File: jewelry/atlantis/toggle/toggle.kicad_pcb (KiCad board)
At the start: 2 copper layers, 24 x 24 mm, 11 parts, among them Q1 Q_PMOS_DGS, U1 74LVC2G04

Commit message: atlantis: Rough PCB for earthing
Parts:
- removed R3: R, Resistor_SMD:R_0603_1608Metric_Pad1.05x0.95mm_HandSolder
- added D10: LED, LED_SMD:LED_0603_1608Metric_Pad1.05x0.95mm_HandSolder, F.Cu at (94.0, 64.8)
- added D11: LED, LED_SMD:LED_0603_1608Metric_Pad1.05x0.95mm_HandSolder, F.Cu at (97.8, 62.2)
- added D12: LED, LED_SMD:LED_0603_1608Metric_Pad1.05x0.95mm_HandSolder, F.Cu at (102.9, 62.2)
- added D4: LED, LED_SMD:LED_0603_1608Metric_Pad1.05x0.95mm_HandSolder, F.Cu at (77.5, 85.5)
- added D5: LED, LED_SMD:LED_0603_1608Metric_Pad1.05x0.95mm_HandSolder, F.Cu at (78.7, 80.9)
- added D6: LED, LED_SMD:LED_0603_1608Metric_Pad1.05x0.95mm_HandSolder, F.Cu at (81.3, 77.5)
- added D7: LED, LED_SMD:LED_0603_1608Metric_Pad1.05x0.95mm_HandSolder, F.Cu at (83.8, 73.7)
- added D8: LED, LED_SMD:LED_0603_1608Metric_Pad1.05x0.95mm_HandSolder, F.Cu at (86.4, 69.8)
- added D9: LED, LED_SMD:LED_0603_1608Metric_Pad1.05x0.95mm_HandSolder, F.Cu at (88.9, 66.9)
- added L1: L, Inductor_SMD:L_1206_3216Metric_Pad1.42x1.75mm_HandSolder, F.Cu at (92.7, 118.1)
- added SW1: SW_SPST, Button_Switch_SMD:SW_SPST_B3S-1000, F.Cu at (80.0, 111.8)
- BT1: value Battery_Cell -> CR1216; footprint Battery:Battery_Panasonic_CR1220-VCN_Vertical_CircularHoles -> touchled:Battery_CR1225
- C1: value 1nF -> 1uF
- C2: value 100nF -> 1uF
- Q1: value Q_PMOS_DGS -> BSS138L
- R1: value 10k -> 100k
- R2: value 100k -> 220R
- U1: value 74LVC2G04 -> AP3019A; footprint Package_TO_SOT_SMD:SOT-23-6_Handsoldering -> touchled:SOT-223-6-extraspace
- moved U1 40.4 mm to (98.0, 117.3), turned to 145 degrees
- moved R2 37.2 mm to (101.6, 119.4), turned to 235 degrees
- moved BT1 35.4 mm to (115.6, 66.0), turned to 315 degrees
- moved C2 32.2 mm to (99.1, 114.3), turned to 325 degrees
- moved Q1 30.7 mm to (89.7, 111.7), turned to 145 degrees
- moved C1 30.0 mm to (88.9, 115.6), turned to 145 degrees
- moved R1 29.3 mm to (94.7, 115.0), turned to 55 degrees
- moved D1 21.4 mm to (77.5, 101.2), turned to 300 degrees
- moved D3 18.6 mm to (77.5, 90.2), turned to 270 degrees
- moved D2 9.39 mm to (77.5, 95.2), turned to 290 degrees
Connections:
- BT1 pad 2: GND -> Net-(BT1-Pad2)
- C1 pad 1: Net-(C1-Pad1) -> VCC
- C2 pad 1: Net-(C2-Pad1) -> /LED+
- D1 pad 1: GND -> Net-(D1-Pad1)
- D1 pad 2: Net-(D1-Pad2) -> /LED+
- D2 pad 1: GND -> Net-(D1-Pad1)
- D2 pad 2: Net-(D1-Pad2) -> /LED+
- D3 pad 1: GND -> Net-(D3-Pad1)
- D3 pad 2: Net-(D1-Pad2) -> Net-(D1-Pad1)
- Q1 pad 1: Net-(BT1-Pad1) -> GND
- Q1 pad 2: GND -> Net-(BT1-Pad2)
- Q1 pad 3: VCC -> Net-(BT1-Pad1)
- R1 pad 1: /OUT -> VCC
- R1 pad 2: Net-(C1-Pad1) -> Net-(R1-Pad2)
- R2 pad 1: Net-(R2-Pad1) -> /LED-
- R2 pad 2: Net-(C2-Pad1) -> GND
- U1 pad 1: Net-(C1-Pad1) -> Net-(L1-Pad2)
- U1 pad 3: Net-(R2-Pad1) -> /LED-
- U1 pad 4: /OUT -> Net-(R1-Pad2)
- U1 pad 5: VCC -> /LED+
- U1 pad 6: Net-(R2-Pad1) -> VCC
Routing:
- net GND: track 0.00 -> 32.3 mm
- net /LED+: track 0.00 -> 30.5 mm
- net Net-(D1-Pad1): track 0.00 -> 15.6 mm
- net Net-(D10-Pad1): track 0.00 -> 15.6 mm
- net Net-(D3-Pad1): track 0.00 -> 14.2 mm
- net Net-(D5-Pad1): track 0.00 -> 13.7 mm
- net Net-(D10-Pad2): track 0.00 -> 13.3 mm
- net VCC: track 0.00 -> 8.44 mm
- net Net-(D11-Pad1): track 0.00 -> 6.43 mm
- net Net-(L1-Pad2): track 0.00 -> 4.52 mm
- net /LED-: track 0.00 -> 3.01 mm
- net Net-(R1-Pad2): track 0.00 -> 2.79 mm
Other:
- board size 24 x 24 mm -> 49.4 x 67.3 mm

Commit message: atlantis: More rough PCB
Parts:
- SW1: footprint Button_Switch_SMD:SW_SPST_B3S-1000 -> Button_Switch_SMD:SW_SPDT_PCM12
- moved SW1 1.27 mm to (81.3, 111.8), turned to 325 degrees
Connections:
- D11 pad 1: Net-(D11-Pad1) -> /LED-
- D12 pad 1: Net-(D11-Pad1) -> /LED-
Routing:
- net /LED-: track 3.01 -> 79.9 mm
- net Net-(D11-Pad1): track 6.43 -> 0.00 mm
- net /LED+: track 30.5 -> 31.6 mm
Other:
- net class Default: clearance 0.2 -> 0.4; trace_width 0.25 -> 0.4
- rule trace_clearance: 0.2 -> 0.4

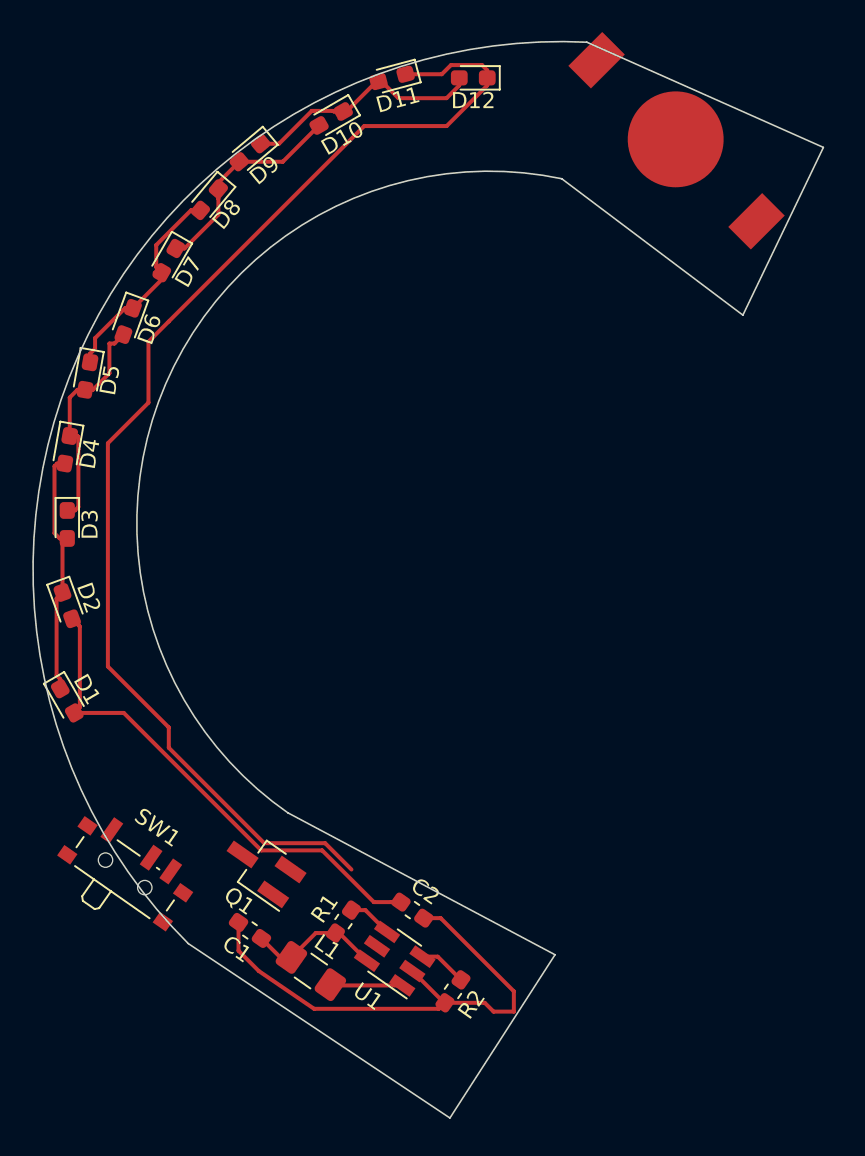
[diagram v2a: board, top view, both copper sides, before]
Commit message: atlantis: Backimport PCB for earthing
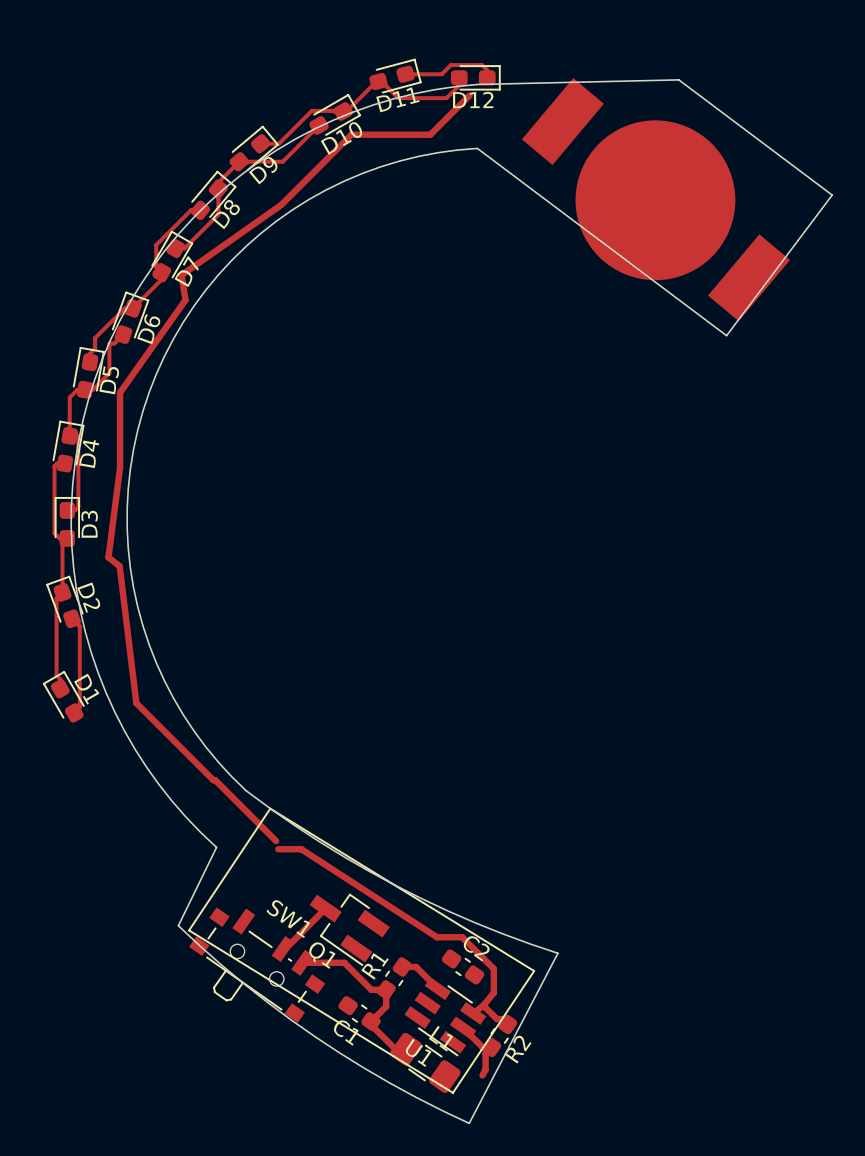
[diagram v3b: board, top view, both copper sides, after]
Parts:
- SW1: value SW_SPST -> SW_SPDT
- moved SW1 10.0 mm to (89.5, 117.5)
- moved L1 9.19 mm to (99.9, 123.9)
- moved C1 8.61 mm to (95.8, 120.8)
- moved Q1 6.21 mm to (94.9, 115.1)
- moved C2 4.77 mm to (102.2, 117.9)
- moved R1 4.77 mm to (97.9, 118.6)
- moved U1 4.77 mm to (101.1, 120.9)
- moved R2 4.04 mm to (104.5, 122.2)
- moved BT1 4.02 mm to (114.3, 69.8), turned to 320 degrees
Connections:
- SW1 pad 1: Net-(BT1-Pad1) -> Net-(SW1-Pad1)
- SW1 pad 2: VCC -> Net-(BT1-Pad1)
- SW1 pad 3: (no net) -> VCC
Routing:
- net GND: track 32.3 -> 4.25 mm
- net /LED+: track 31.6 -> 6.24 mm
- net /LED-: track 79.9 -> 90.4 mm
- net Net-(L1-Pad2): track 4.52 -> 0.00 mm
- net Net-(BT1-Pad1): track 0.00 -> 3.72 mm
- net VCC: track 8.44 -> 11.2 mm
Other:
- board size 49.4 x 67.3 mm -> 47.6 x 65.3 mm

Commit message: atlantis: Earthing PCB near ready
Just positioning and routing of LEDs
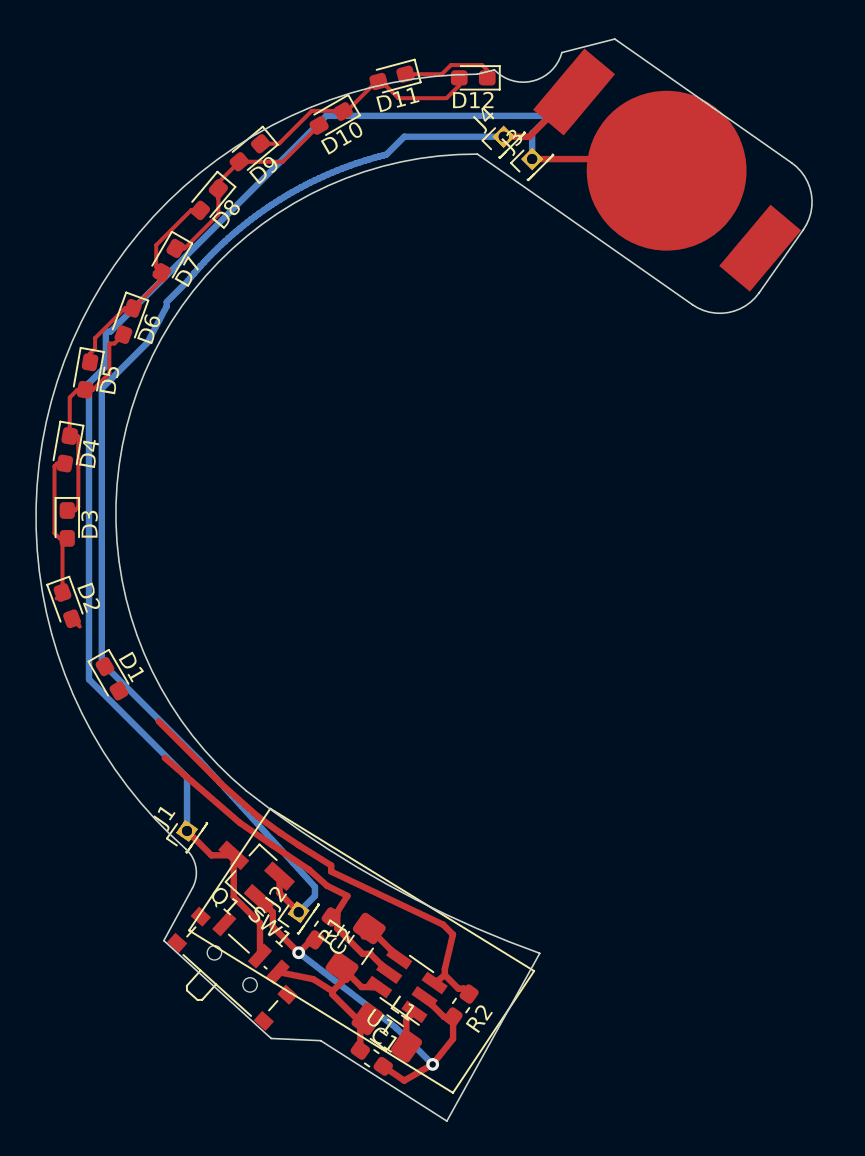
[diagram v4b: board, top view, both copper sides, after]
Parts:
- added J1: Conn_01x01, Connector_PinHeader_1.27mm:PinHeader_1x01_P1.27mm_Vertical, F.Cu at (85.0, 109.3)
- added J2: Conn_01x01, Connector_PinHeader_1.27mm:PinHeader_1x01_P1.27mm_Vertical, F.Cu at (91.9, 114.4)
- added J3: Conn_01x01, Connector_PinHeader_1.27mm:PinHeader_1x01_P1.27mm_Vertical, F.Cu at (106.6, 67.3)
- added J4: Conn_01x01, Connector_PinHeader_1.27mm:PinHeader_1x01_P1.27mm_Vertical, F.Cu at (104.8, 65.9)
- R1: footprint Resistor_SMD:R_0603_1608Metric_Pad1.05x0.95mm_HandSolder -> Resistor_SMD:R_1206_3216Metric_Pad1.42x1.75mm_HandSolder
- moved C2 9.09 mm to (93.5, 115.4), turned to 235 degrees
- moved Q1 6.68 mm to (89.0, 111.9), turned to 138 degrees
- moved D1 3.12 mm to (80.3, 99.8)
- moved L1 3.07 mm to (97.5, 122.0)
- moved R2 3.07 mm to (102.1, 120.3)
- moved U1 3.07 mm to (98.7, 119.0)
- moved R1 3.07 mm to (95.5, 116.7)
- moved C1 2.90 mm to (96.5, 123.6), turned to 325 degrees
- moved BT1 1.98 mm to (115.0, 68.0)
- moved SW1 1.55 mm to (88.0, 117.7), turned to 318 degrees
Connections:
- net Net-(BT1-Pad1) renamed /BATT+
- net Net-(BT1-Pad2) renamed /BATT-
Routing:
- net /BATT+: track 3.72 -> 90.0 mm
- net /BATT-: track 0.00 -> 78.4 mm
- net /LED-: track 90.4 -> 34.5 mm
- net GND: track 4.25 -> 26.0 mm, vias 0 -> 2
- net /LED+: track 6.24 -> 21.7 mm
- net Net-(D1-Pad1): track 15.6 -> 9.88 mm
- net VCC: track 11.2 -> 13.8 mm
- net Net-(L1-Pad2): track 0.00 -> 2.36 mm
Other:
- board size 47.6 x 65.3 mm -> 48.5 x 67.7 mm

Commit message: atlantis: Earthing PCB ready for test?
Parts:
- moved D12 4.12 mm to (99.4, 64.5), turned to 10 degrees
- moved D11 4.02 mm to (95.5, 65.5), turned to 20 degrees
- moved D10 3.42 mm to (91.7, 67.3), turned to 28 degrees
- moved D8 2.56 mm to (85.2, 72.1), turned to 45 degrees
- moved D9 2.48 mm to (88.4, 69.3), turned to 37 degrees
- moved D7 2.08 mm to (82.5, 75.3), turned to 55 degrees
- moved D5 1.94 mm to (79.0, 82.8), turned to 75 degrees
- moved D4 1.63 mm to (78.1, 87.0), turned to 83 degrees
- moved D6 1.59 mm to (80.5, 78.9), turned to 65 degrees
- moved D1 1.08 mm to (79.5, 99.1), turned to 110 degrees
- moved D3 1.02 mm to (78.0, 91.1), turned to 90 degrees
- moved J2 0.99 mm to (92.6, 113.7)
- moved D2 0.90 mm to (78.4, 95.1), turned to 100 degrees
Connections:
- D1 pad 1: Net-(D1-Pad1) -> /LED-
- D1 pad 2: /LED+ -> Net-(D1-Pad2)
- D11 pad 1: /LED- -> Net-(D10-Pad2)
- D11 pad 2: Net-(D10-Pad1) -> /LED+
- D12 pad 1: /LED- -> Net-(D10-Pad2)
- D12 pad 2: Net-(D10-Pad1) -> /LED+
- D2 pad 1: Net-(D1-Pad1) -> /LED-
- D2 pad 2: /LED+ -> Net-(D1-Pad2)
- D3 pad 1: Net-(D3-Pad1) -> Net-(D1-Pad2)
- D3 pad 2: Net-(D1-Pad1) -> Net-(D3-Pad2)
- D4 pad 1: Net-(D3-Pad1) -> Net-(D1-Pad2)
- D4 pad 2: Net-(D1-Pad1) -> Net-(D3-Pad2)
- D5 pad 1: Net-(D5-Pad1) -> Net-(D3-Pad2)
- D5 pad 2: Net-(D3-Pad1) -> Net-(D5-Pad2)
- D6 pad 1: Net-(D5-Pad1) -> Net-(D3-Pad2)
- D6 pad 2: Net-(D3-Pad1) -> Net-(D5-Pad2)
- D7 pad 1: Net-(D10-Pad2) -> Net-(D5-Pad2)
- D7 pad 2: Net-(D5-Pad1) -> Net-(D10-Pad1)
- D8 pad 1: Net-(D10-Pad2) -> Net-(D5-Pad2)
- D8 pad 2: Net-(D5-Pad1) -> Net-(D10-Pad1)
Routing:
- net /LED+: track 21.7 -> 90.2 mm, vias 0 -> 2
- net Net-(D3-Pad1): track 14.2 -> 0.00 mm
- net Net-(D5-Pad1): track 13.7 -> 0.00 mm
- net Net-(D3-Pad2): track 0.00 -> 13.3 mm
- net Net-(D5-Pad2): track 0.00 -> 13.3 mm
- net Net-(D1-Pad2): track 0.00 -> 13.0 mm
- net Net-(D1-Pad1): track 9.88 -> 0.00 mm
- net /LED-: track 34.5 -> 38.2 mm
- net Net-(D10-Pad1): track 15.6 -> 12.6 mm
- net /BATT-: track 78.4 -> 76.5 mm
- net GND: track 26.0 -> 27.6 mm

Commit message: atlantis: Earthing CAD ready for first test
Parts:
- moved SW1 0.18 mm to (87.9, 117.9)
- turned BT1 to 325 degrees
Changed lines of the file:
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@@
   )
   (module touchled:Battery_CR1225 (layer F.Cu)
-    (at 115 68 320)
+    (at 115 68 325)
     (descr "CR1225 battery")
     (tags "battery CR1225 coin cell")
     (attr virtual)
-    (fp_text reference BT1 (at 0.000001 -1 140) (layer F.SilkS) hide
-      (effects (font (size 1 1) (thickness 0.15)))
-    )
-    (fp_text value CR1216 (at 0 0.499999 140) (layer F.Fab)
+    (fp_text reference BT1 (at 0.000001 -1 145) (layer F.SilkS) hide
+      (effects (font (size 1 1) (thickness 0.15)))
+    )
+    (fp_text value CR1216 (at 0 0.499999 145) (layer F.Fab)
       (effects (font (size 1 1) (thickness 0.15)))
     )
     (fp_circle (center 0 0) (end 7 0) (layer F.CrtYd) (width 0.1))
-    (pad 2 smd rect (at 7.6 0 320) (size 2.5 5) (layers F.Cu F.Paste F.Mask)
-      (net 11 /BATT-))
-    (pad 2 smd rect (at -7.6 0 320) (size 2.5 5) (layers F.Cu F.Paste F.Mask)
-      (net 11 /BATT-))
-    (pad 1 smd circle (at 0 0.05 320) (size 10 10) (layers F.Cu F.Paste F.Mask)
+    (pad 2 smd rect (at 7.6 0 325) (size 2.5 5) (layers F.Cu F.Paste F.Mask)
+      (net 11 /BATT-))
+    (pad 2 smd rect (at -7.6 0 325) (size 2.5 5) (layers F.Cu F.Paste F.Mask)
+      (net 11 /BATT-))
+    (pad 1 smd circle (at 0 0.05 325) (size 10 10) (layers F.Cu F.Paste F.Mask)
       (net 12 /BATT+))
     (model /home/jon/projects/personal/jewelry/atlantis/batth-cr1220.step
@@
   )
   (module Button_Switch_SMD:SW_SPDT_PCM12 (layer F.Cu)
-    (at 88.011 117.729 318)
+    (at 87.884 117.856 318)
     (descr "Ultraminiature Surface Mount Slide Switch, right-angle, https://www.ckswitches.com/media/1424/pcm.pdf")
     (attr smd)

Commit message: atlantis: Adjusted PCB
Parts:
- D1, D10, D11, D12, D2, D3, D4, D5, D6, D7, D8, D9: footprint LED_SMD:LED_0603_1608Metric_Pad1.05x0.95mm_HandSolder -> touchled:LED_0603_bigger
- J1, J2, J3, J4: footprint Connector_PinHeader_1.27mm:PinHeader_1x01_P1.27mm_Vertical -> touchled:PinHeader
- moved J2 6.08 mm to (87.2, 110.7), turned to 145 degrees
- moved Q1 1.65 mm to (90.2, 113.0), turned to 318 degrees
- moved J1 1.48 mm to (85.7, 108.1)
- moved J3 0.18 mm to (106.4, 67.4)
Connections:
- Q1 pad 1: GND -> /BATT+
- Q1 pad 3: /BATT+ -> GND
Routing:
- net /BATT+: track 89.7 -> 94.5 mm
- net /BATT-: track 76.5 -> 73.1 mm
- net Net-(D10-Pad2): track 13.1 -> 15.7 mm
- net Net-(D10-Pad1): track 12.6 -> 15.0 mm
- net Net-(D5-Pad2): track 13.3 -> 15.5 mm
- net Net-(D3-Pad2): track 13.3 -> 15.5 mm
- net Net-(D1-Pad2): track 13.0 -> 15.0 mm
- net /LED+: track 90.2 -> 91.8 mm
- net /LED-: track 38.2 -> 39.4 mm

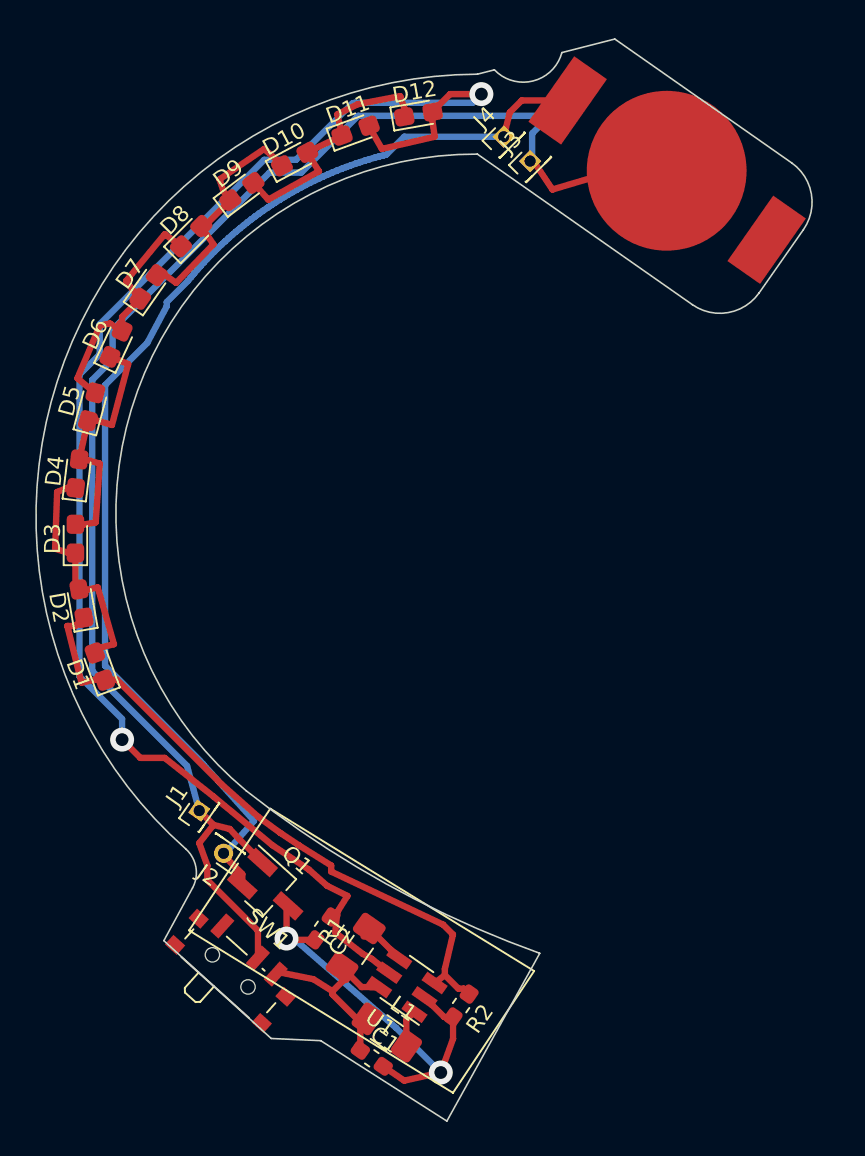
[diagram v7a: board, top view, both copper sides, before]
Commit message: atlantis: Fix batt holder and NMOS wrong direction
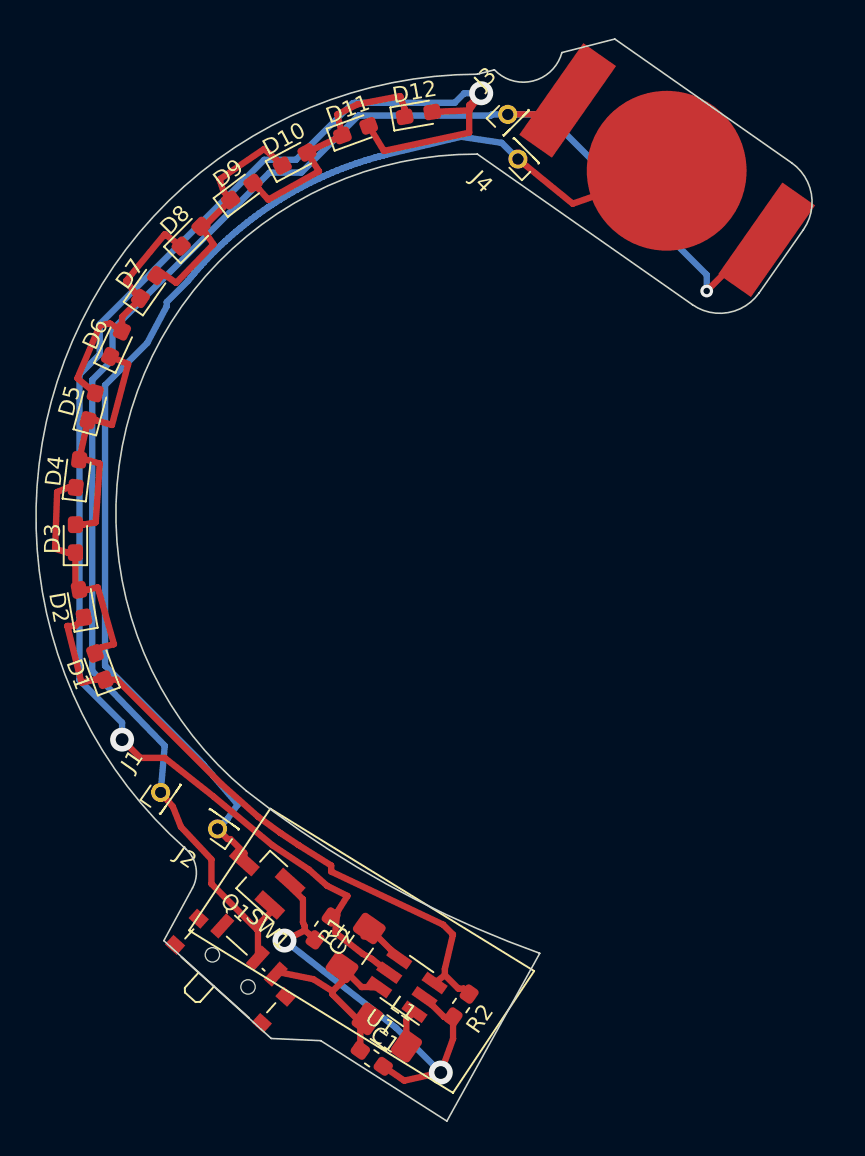
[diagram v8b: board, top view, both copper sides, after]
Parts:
- D1, D10, D11, D12, D2, D3, D4, D5, D6, D7, D8, D9: footprint touchled:LED_0603_bigger -> LED_SMD:LED_0603_1608Metric_Pad1.05x0.95mm_HandSolder
- moved J3 3.24 mm to (105.0, 64.5)
- moved J1 2.67 mm to (83.3, 106.9)
- moved J4 1.66 mm to (105.7, 67.3), turned to 135 degrees
- moved J2 1.57 mm to (86.9, 109.2)
- moved Q1 0.92 mm to (89.7, 112.3), turned to 138 degrees
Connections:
- Q1 pad 2: /BATT- -> GND
- Q1 pad 3: GND -> /BATT-
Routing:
- net /BATT+: track 94.5 -> 102.8 mm, vias 0 -> 1
- net /BATT-: track 73.1 -> 78.4 mm
- net /LED+: track 91.8 -> 95.3 mm
- net GND: track 27.2 -> 28.1 mm
